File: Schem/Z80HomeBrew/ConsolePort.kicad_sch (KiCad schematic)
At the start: 12 parts, among them J16 Conn_01x04, J3 0480370001, U14 FT230XS-U

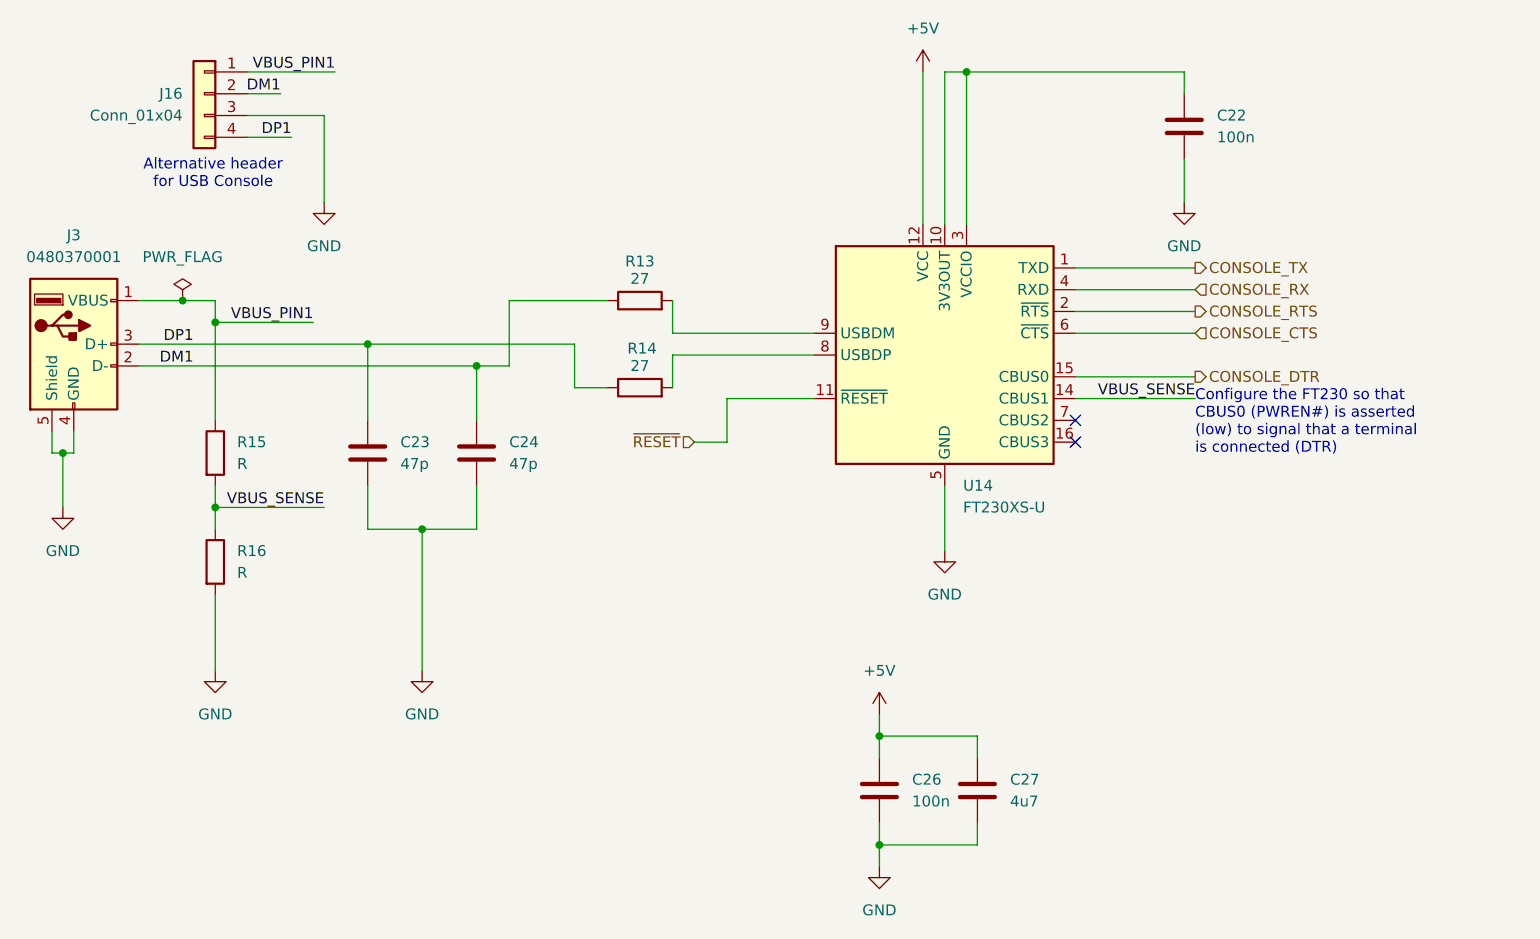
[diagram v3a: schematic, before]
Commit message: Added pBITzBackplane and MezzanineConnector
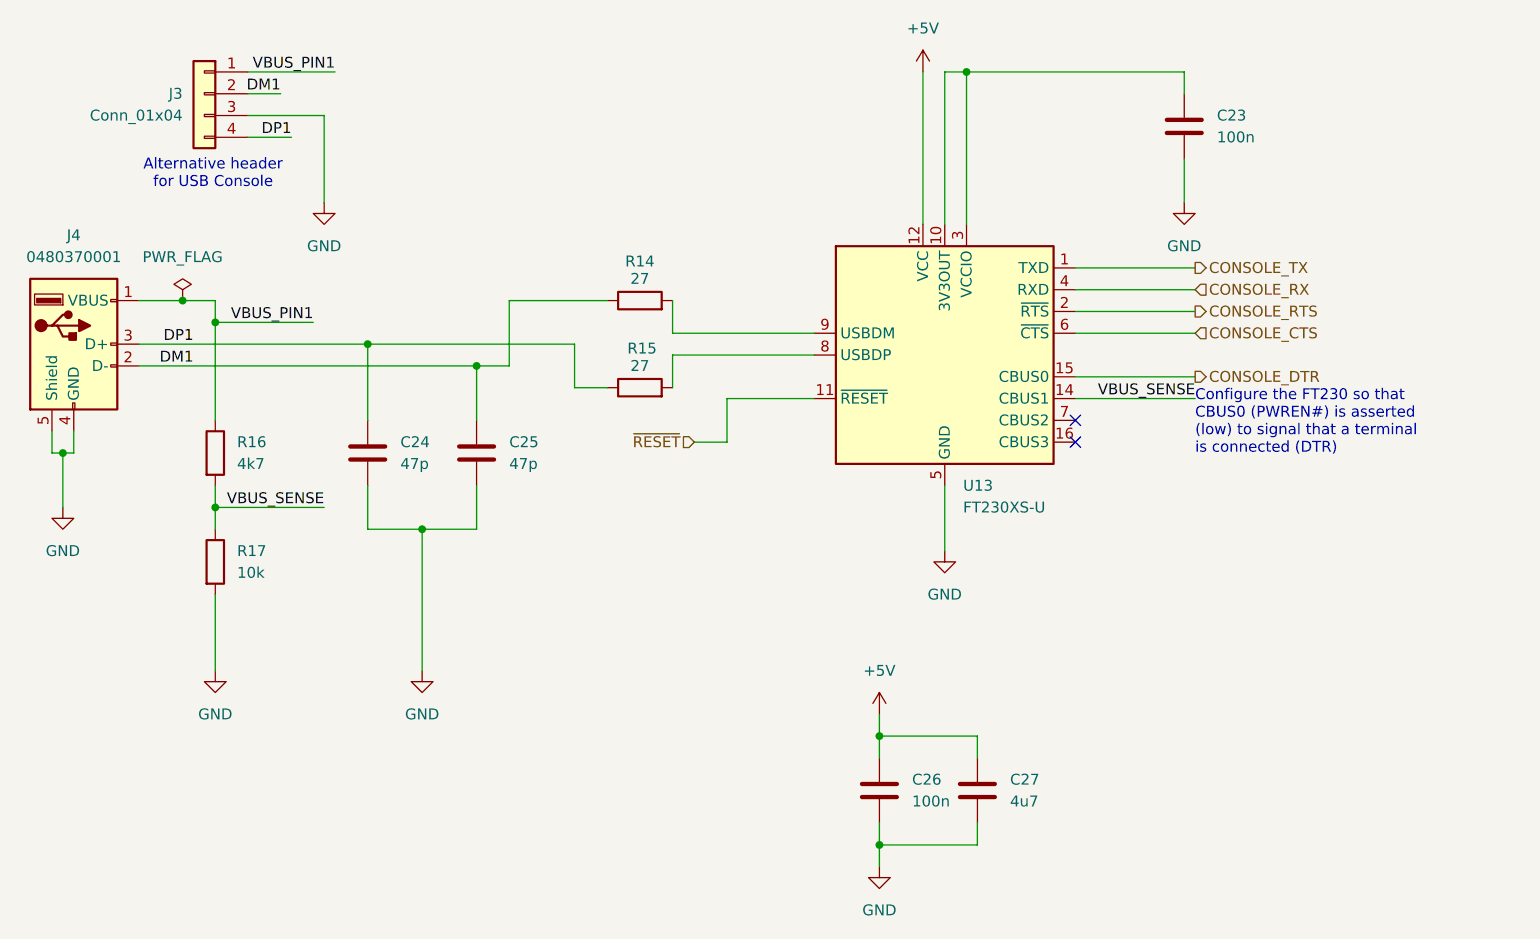
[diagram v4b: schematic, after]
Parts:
- C23: renamed from C22; MANUFACTURER_PART_NUMBER (none) -> C0603C104K5RACTU
- C24: renamed from C23; MANUFACTURER_PART_NUMBER (none) -> 885012006021
- C25: renamed from C24; MANUFACTURER_PART_NUMBER (none) -> 885012006021
- C26: MANUFACTURER_PART_NUMBER (none) -> C0603C104K5RACTU
- C27: MANUFACTURER_PART_NUMBER (none) -> CL10A475KP8NNNC
- J3: renamed from J16; MANUFACTURER_PART_NUMBER (none) -> 732-5301-ND
- J4: renamed from J3; MANUFACTURER_PART_NUMBER (none) -> MSD-1-A
- R14: renamed from R13; MANUFACTURER_PART_NUMBER (none) -> RC0603FR-0727RL
- R15: renamed from R14; MANUFACTURER_PART_NUMBER (none) -> RC0603FR-0727RL
- R16: renamed from R15; value R -> 4k7; MANUFACTURER_PART_NUMBER (none) -> CRCW06034K70FKEA
- R17: renamed from R16; value R -> 10k; MANUFACTURER_PART_NUMBER (none) -> RC0603FR-0710KL
- U13: renamed from U14; MANUFACTURER_PART_NUMBER (none) -> FT230XS-U
